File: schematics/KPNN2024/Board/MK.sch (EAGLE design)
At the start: 7 parts

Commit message: ПОМЕЛО
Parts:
- added U$2: SWITCH_MSS, UNKNOWN-2024:SWITCH_MSS
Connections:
- new net ADC0: U$1.PA0
- new net D0_SD: U$1.PB7
- new net SCL1: U$1.PB6
- new net SDA_BME: U$1.PB9
- new net SWITCH: U$1.PB1, U$2.P
- net 3V3: now also U$2.S
- net CE_RADIO: now also U$1.PC13; no longer U$1.PC15
- net D0: no longer U$1.PB7
- net GND: now also U$2.O
- net SCL: no longer U$1.PB6
- net SDA: no longer U$1.PB9

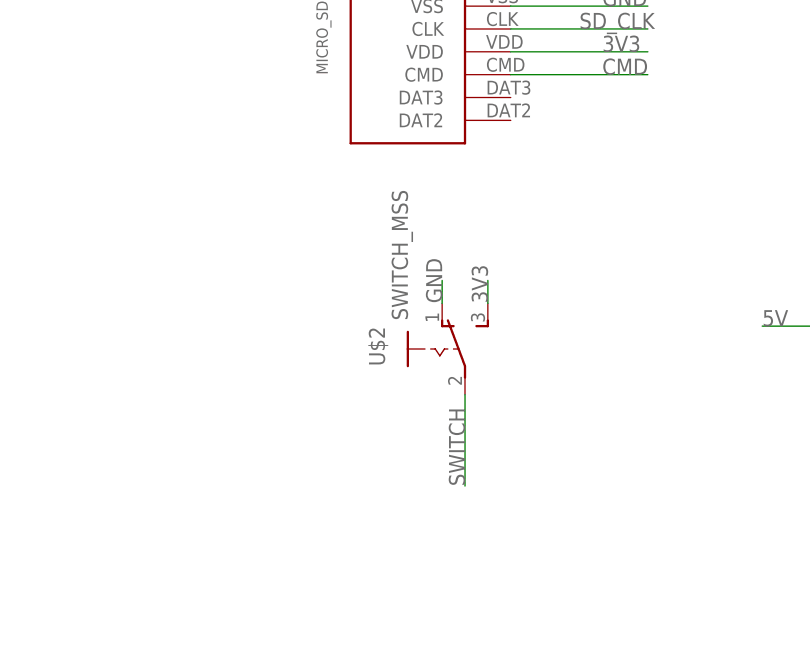
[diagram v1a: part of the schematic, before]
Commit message: Добавлены УГО радио и разъемов радиолинии
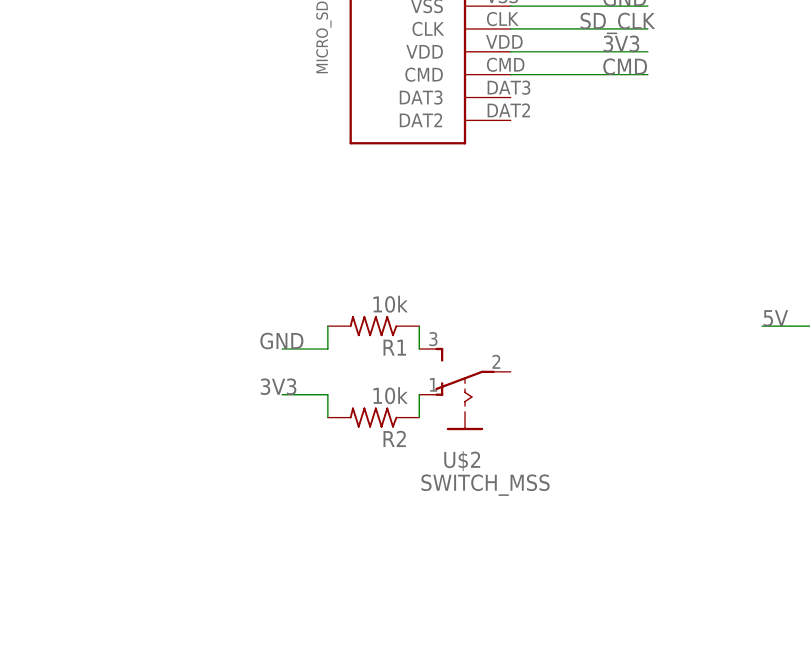
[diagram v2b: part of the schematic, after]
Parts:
- added R1, R2: 10k, rcl:R-US_R0603
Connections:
- new net N$1: R1.1, U$2.S
- new net N$2: R2.1, U$2.O
- net 3V3: now also R2.2; no longer U$2.S
- net GND: now also R1.2; no longer U$2.O
- net SWITCH: no longer U$2.P
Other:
- moved on the sheet: U$2
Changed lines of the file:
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@@
 <part name="R10" library="rcl" library_urn="urn:adsk.eagle:library:334" deviceset="R-US_" device="R0603" package3d_urn="urn:adsk.eagle:package:23555/3" value="100R"/>
 <part name="U$2" library="UNKNOWN-2024" deviceset="SWITCH_MSS" device=""/>
+<part name="R1" library="rcl" library_urn="urn:adsk.eagle:library:334" deviceset="R-US_" device="R0603" package3d_urn="urn:adsk.eagle:package:23555/3" value="10k"/>
+<part name="R2" library="rcl" library_urn="urn:adsk.eagle:library:334" deviceset="R-US_" device="R0603" package3d_urn="urn:adsk.eagle:package:23555/3" value="10k"/>
 </parts>
 <sheets>
@@
 <attribute name="VALUE" x="234.442" y="41.91" size="1.778" layer="96" rot="R90"/>
 </instance>
-<instance part="U$2" gate="G$1" x="142.24" y="60.96" smashed="yes">
-<attribute name="NAME" x="135.89" y="59.055" size="1.778" layer="95" rot="R90"/>
-<attribute name="VALUE" x="138.43" y="64.135" size="1.778" layer="96" rot="R90"/>
+<instance part="U$2" gate="G$1" x="144.78" y="55.88" smashed="yes" rot="R90">
+<attribute name="NAME" x="146.685" y="49.53" size="1.778" layer="95" rot="R180"/>
+<attribute name="VALUE" x="154.305" y="46.99" size="1.778" layer="96" rot="R180"/>
+</instance>
+<instance part="R1" gate="G$1" x="134.62" y="63.5" smashed="yes" rot="R180">
+<attribute name="NAME" x="138.43" y="62.0014" size="1.778" layer="95" rot="R180"/>
+<attribute name="VALUE" x="138.43" y="66.802" size="1.778" layer="96" rot="R180"/>
+</instance>
+<instance part="R2" gate="G$1" x="134.62" y="53.34" smashed="yes" rot="R180">
+<attribute name="NAME" x="138.43" y="51.8414" size="1.778" layer="95" rot="R180"/>
+<attribute name="VALUE" x="138.43" y="56.642" size="1.778" layer="96" rot="R180"/>
 </instance>
 </instances>
@@
 </segment>
 <segment>
-<pinref part="U$2" gate="G$1" pin="O"/>
-<wire x1="142.24" y1="66.04" x2="142.24" y2="68.58" width="0.1524" layer="91"/>
-<label x="142.24" y="66.04" size="1.778" layer="95" rot="R90"/>
+<pinref part="R1" gate="G$1" pin="2"/>
+<wire x1="129.54" y1="63.5" x2="129.54" y2="60.96" width="0.1524" layer="91"/>
+<wire x1="129.54" y1="60.96" x2="124.46" y2="60.96" width="0.1524" layer="91"/>
+<label x="121.92" y="60.96" size="1.778" layer="95"/>
 </segment>
 </net>
@@
 </segment>
 <segment>
-<pinref part="U$2" gate="G$1" pin="S"/>
-<wire x1="147.32" y1="66.04" x2="147.32" y2="68.58" width="0.1524" layer="91"/>
-<label x="147.32" y="66.04" size="1.778" layer="95" rot="R90"/>
+<pinref part="R2" gate="G$1" pin="2"/>
+<wire x1="129.54" y1="53.34" x2="129.54" y2="55.88" width="0.1524" layer="91"/>
+<wire x1="129.54" y1="55.88" x2="124.46" y2="55.88" width="0.1524" layer="91"/>
+<label x="121.92" y="55.88" size="1.778" layer="95"/>
 </segment>
 </net>
@@
 <label x="0" y="96.52" size="1.778" layer="95"/>
 </segment>
-<segment>
-<pinref part="U$2" gate="G$1" pin="P"/>
-<wire x1="144.78" y1="55.88" x2="144.78" y2="45.72" width="0.1524" layer="91"/>
-<label x="144.78" y="45.72" size="1.778" layer="95" rot="R90"/>
-</segment>
-</net>
+</net>
+<net name="N$1" class="0">
+<segment>
+<pinref part="R1" gate="G$1" pin="1"/>
+<pinref part="U$2" gate="G$1" pin="S"/>
+<wire x1="139.7" y1="63.5" x2="139.7" y2="60.96" width="0.1524" layer="91"/>
+</segment>
+</net>
+<net name="N$2" class="0">
+<segment>
+<pinref part="R2" gate="G$1" pin="1"/>
+<pinref part="U$2" gate="G$1" pin="O"/>
+<wire x1="139.7" y1="53.34" x2="139.7" y2="55.88" width="0.1524" layer="91"/>
+</segment>
+</net>
